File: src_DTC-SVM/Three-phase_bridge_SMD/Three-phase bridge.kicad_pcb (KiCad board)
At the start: 2 copper layers, 419.1 x 318 mm, 92 parts, among them M1 MCP6022-I/P, M2 MCP6022-I/P, P1 CONN_1, P2 POWER_FUSE, P3 CONN_2, P4 CONN_1, P5 CONN_1, P6 POWER_FUSE

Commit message: Commiting...
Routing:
- net +48V: track 185.1 -> 276.9 mm
- net N-0000026: track 18.3 -> 63.0 mm, vias 0 -> 1
- net GND: track 489.9 -> 506.0 mm
- net VCC: track 140.0 -> 146.8 mm
- net N-0000046: track 0.00 -> 2.17 mm
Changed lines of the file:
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@@
   (general
     (links 262)
-    (no_connects 55)
+    (no_connects 50)
     (area -125.780001 -108.254001 293.420001 219.695888)
     (thickness 1.6)
     (drawings 8)
-    (tracks 821)
+    (tracks 855)
     (zones 0)
     (modules 92)
@@
   (segment (start 179.197 116.713) (end 179.197 127.381) (width 1.905) (layer B.Cu) (net 1))
   (segment (start 178.181 115.697) (end 179.197 116.713) (width 1.905) (layer B.Cu) (net 1))
+  (segment (start 217.297 94.869) (end 218.059 94.869) (width 1.905) (layer F.Cu) (net 2))
+  (segment (start 216.154 93.726) (end 217.297 94.869) (width 1.905) (layer F.Cu) (net 2) (status 400000))
+  (segment (start 215.265 93.726) (end 216.154 93.726) (width 1.905) (layer F.Cu) (net 2) (status C00000))
+  (segment (start 218.059 94.869) (end 221.7674 91.1606) (width 1.905) (layer F.Cu) (net 2))
+  (segment (start 215.265 93.726) (end 216.789 93.726) (width 1.905) (layer F.Cu) (net 2) (status 400000))
+  (segment (start 221.7674 92.837) (end 221.7674 93.7006) (width 1.905) (layer F.Cu) (net 2))
+  (segment (start 217.678 92.837) (end 221.7674 92.837) (width 1.905) (layer F.Cu) (net 2))
+  (segment (start 216.789 93.726) (end 217.678 92.837) (width 1.905) (layer F.Cu) (net 2))
+  (segment (start 221.7674 93.7006) (end 221.7674 93.7006) (width 1.905) (layer F.Cu) (net 2))
+  (segment (start 220.218 86.741) (end 220.853 86.741) (width 7.62) (layer F.Cu) (net 2))
+  (segment (start 220.853 86.741) (end 221.7674 87.6554) (width 7.62) (layer F.Cu) (net 2))
+  (segment (start 221.7674 87.6554) (end 221.7674 91.1606) (width 7.62) (layer F.Cu) (net 2))
+  (segment (start 182.8546 71.7296) (end 152.4762 71.7296) (width 7.62) (layer F.Cu) (net 2) (status 800000))
+  (segment (start 220.218 86.487) (end 220.218 86.741) (width 7.62) (layer F.Cu) (net 2))
+  (segment (start 217.932 84.201) (end 220.218 86.487) (width 7.62) (layer F.Cu) (net 2))
+  (segment (start 195.326 84.201) (end 217.932 84.201) (width 7.62) (layer F.Cu) (net 2))
+  (segment (start 182.8546 71.7296) (end 195.326 84.201) (width 7.62) (layer F.Cu) (net 2))
+  (segment (start 221.7674 91.1606) (end 221.7674 93.7006) (width 7.62) (layer F.Cu) (net 2))
   (segment (start 133.3754 80.0862) (end 134.4676 80.0862) (width 1.016) (layer F.Cu) (net 2))
   (segment (start 134.9248 79.629) (end 134.9248 74.0156) (width 1.016) (layer F.Cu) (net 2))
@@
   (segment (start 134.9248 74.0156) (end 134.9248 75.2348) (width 1.016) (layer F.Cu) (net 2))
   (segment (start 134.747 70.739) (end 134.9248 70.9168) (width 1.016) (layer F.Cu) (net 2))
-  (segment (start 221.742 93.6752) (end 215.3158 93.6752) (width 1.905) (layer F.Cu) (net 2))
-  (segment (start 215.3158 93.6752) (end 215.265 93.726) (width 1.905) (layer F.Cu) (net 2))
-  (segment (start 221.742 93.6752) (end 221.7674 93.7006) (width 7.62) (layer F.Cu) (net 2))
   (segment (start 234.696 205.867) (end 234.696 204.216) (width 1.905) (layer F.Cu) (net 2))
   (segment (start 233.045 202.565) (end 226.949 202.565) (width 1.905) (layer F.Cu) (net 2))
@@
   (segment (start 191.3763 199.0217) (end 191.3763 202.4253) (width 1.905) (layer F.Cu) (net 3))
   (segment (start 191.3763 202.4253) (end 191.4525 202.5015) (width 1.905) (layer F.Cu) (net 3))
+  (segment (start 194.818 113.5126) (end 194.818 112.903) (width 1.016) (layer F.Cu) (net 4) (status 400000))
+  (segment (start 186.2582 106.6038) (end 186.2582 108.0516) (width 1.016) (layer F.Cu) (net 4) (status 800000))
+  (segment (start 186.563 106.299) (end 186.2582 106.6038) (width 1.016) (layer F.Cu) (net 4))
+  (segment (start 192.659 106.299) (end 186.563 106.299) (width 1.016) (layer F.Cu) (net 4))
+  (segment (start 193.294 106.934) (end 192.659 106.299) (width 1.016) (layer F.Cu) (net 4))
+  (segment (start 193.294 111.379) (end 193.294 106.934) (width 1.016) (layer F.Cu) (net 4))
+  (segment (start 194.818 112.903) (end 193.294 111.379) (width 1.016) (layer F.Cu) (net 4))
   (segment (start 183.388 101.727) (end 183.388 107.315) (width 1.016) (layer B.Cu) (net 4) (status 400000))
   (segment (start 183.388 107.315) (end 184.15 108.077) (width 1.016) (layer B.Cu) (net 4) (status 800000))
@@
   (segment (start 174.9171 205.3209) (end 177.43424 205.3209) (width 1.905) (layer F.Cu) (net 11))
   (segment (start 177.43424 205.3209) (end 177.4571 205.34376) (width 1.905) (layer F.Cu) (net 11))
-  (segment (start 150.8252 123.8504) (end 150.8252 120.3198) (width 1.905) (layer F.Cu) (net 12))
-  (segment (start 150.8252 120.3198) (end 152.146 118.999) (width 1.905) (layer F.Cu) (net 12))
+  (segment (start 150.8252 123.8504) (end 150.8252 120.3198) (width 1.905) (layer F.Cu) (net 12) (status C00000))
+  (segment (start 150.8252 120.3198) (end 152.146 118.999) (width 1.905) (layer F.Cu) (net 12) (status C00000))
   (segment (start 166.6367 205.34376) (end 163.99256 205.34376) (width 1.905) (layer F.Cu) (net 13))
   (segment (start 163.99256 205.34376) (end 163.9697 205.3209) (width 1.905) (layer F.Cu) (net 13))
@@
   (segment (start 186.4106 125.73) (end 186.6138 125.9332) (width 1.905) (layer F.Cu) (net 26))
   (segment (start 186.6138 125.9332) (end 188.5696 125.9332) (width 1.905) (layer F.Cu) (net 26))
+  (via (at 197.739 128.016) (size 0.254) (layers F.Cu B.Cu) (net 27))
+  (segment (start 194.818 121.8946) (end 196.1896 121.8946) (width 1.016) (layer F.Cu) (net 27) (status 400000))
+  (segment (start 196.1896 121.8946) (end 197.739 123.444) (width 1.016) (layer F.Cu) (net 27))
+  (segment (start 197.739 128.016) (end 197.739 123.444) (width 1.905) (layer F.Cu) (net 27))
+  (segment (start 206.756 151.257) (end 206.756 160.909) (width 1.905) (layer B.Cu) (net 27) (status 800000))
+  (segment (start 200.152 144.653) (end 206.756 151.257) (width 1.905) (layer B.Cu) (net 27))
+  (segment (start 200.152 130.429) (end 200.152 144.653) (width 1.905) (layer B.Cu) (net 27))
+  (segment (start 197.739 128.016) (end 200.152 130.429) (width 1.905) (layer B.Cu) (net 27))
   (segment (start 199.644 163.449) (end 204.216 163.449) (width 1.016) (layer B.Cu) (net 27))
   (segment (start 204.216 163.449) (end 206.756 160.909) (width 1.016) (layer B.Cu) (net 27))
@@
   (segment (start 154.432 186.563) (end 165.8576 186.563) (width 0.889) (layer B.Cu) (net 48))
   (segment (start 153.1355 185.2665) (end 154.432 186.563) (width 0.889) (layer B.Cu) (net 48))
+  (segment (start 158.877 104.54386) (end 161.01314 104.54386) (width 1.905) (layer F.Cu) (net 49) (status C00000))
+  (segment (start 161.01314 104.54386) (end 161.036 104.521) (width 1.905) (layer F.Cu) (net 49) (status C00000))
   (segment (start 194.691 104.267) (end 196.215 104.267) (width 1.016) (layer B.Cu) (net 50))
   (segment (start 196.215 104.267) (end 200.533 108.585) (width 1.016) (layer B.Cu) (net 50))
@@
   (segment (start 207.6196 148.3614) (end 208.534 147.447) (width 1.905) (layer F.Cu) (net 91))
   (segment (start 188.9506 138.2522) (end 184.3786 138.2522) (width 1.905) (layer F.Cu) (net 92))
+  (segment (start 158.877 101.70414) (end 152.16886 101.70414) (width 1.905) (layer F.Cu) (net 93) (status C00000))
+  (segment (start 152.16886 101.70414) (end 152.146 101.727) (width 1.905) (layer F.Cu) (net 93) (status C00000))
   (segment (start 168.1988 120.4214) (end 168.783 120.4214) (width 1.905) (layer F.Cu) (net 93))
   (segment (start 181.9402 141.5796) (end 183.6928 143.3322) (width 1.905) (layer F.Cu) (net 93))

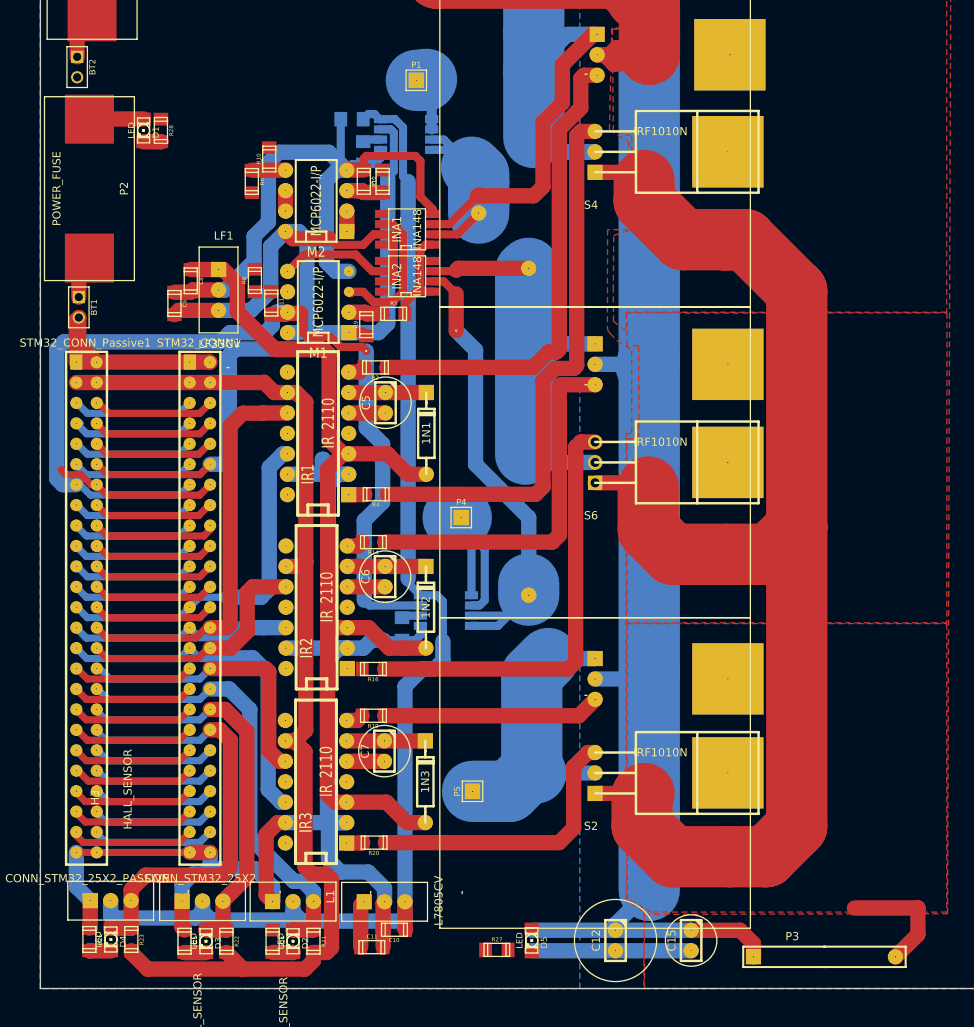
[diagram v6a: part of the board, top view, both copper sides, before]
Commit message: New ADC ports for the hall current sensors have been added to the PCB. Rewiring of surrounding connections is being carried out.
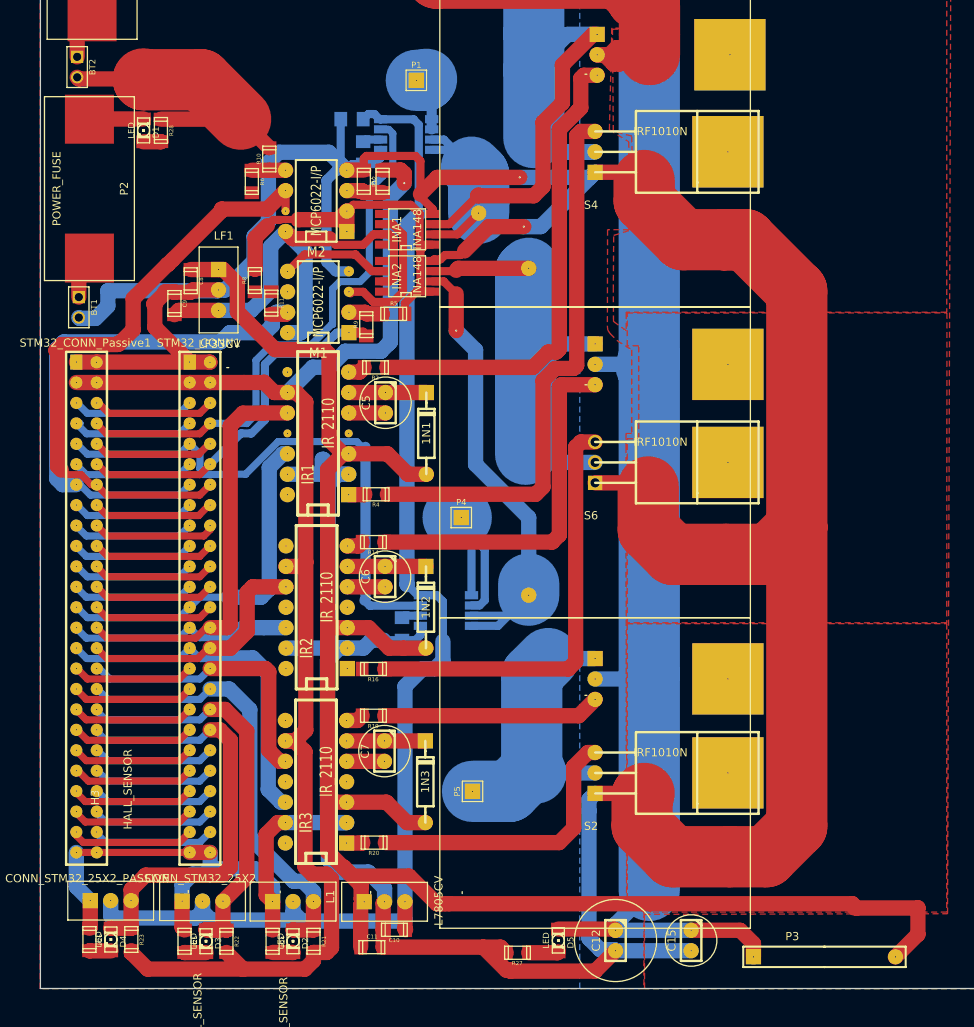
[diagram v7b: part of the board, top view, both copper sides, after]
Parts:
- moved D5 3.30 mm to (210.4, 203.8)
- moved R27 2.59 mm to (205.4, 205.4), turned to 180 degrees
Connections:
- ACS1 pad 7: N-0000065 (its old number) -> N-0000066
- ACS2 pad 7: N-0000034 (its old number) -> N-0000048
- M1 pad 1: N-0000065 (its old number) -> N-0000067
- M1 pad 7: N-0000034 (its old number) -> N-0000037
- R11 pad 1: N-0000034 (its old number) -> N-0000037
- R9 pad 2: N-0000065 (its old number) -> N-0000067
- STM32_CONN1 pad 12: N-0000065 (its old number) -> N-0000067
- STM32_CONN1 pad 13: N-0000034 (its old number) -> N-0000037
- STM32_CONN1 pad 8: N-0000064 (its old number) -> N-0000066
- STM32_CONN1 pad 9: N-0000037 -> N-0000048
- STM32_CONN_Passive1 pad 12: N-0000065 (its old number) -> N-0000067
- STM32_CONN_Passive1 pad 13: N-0000034 (its old number) -> N-0000037
- STM32_CONN_Passive1 pad 8: N-0000064 (its old number) -> N-0000066
- STM32_CONN_Passive1 pad 9: N-0000037 -> N-0000048
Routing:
- net GND: track 506.0 -> 661.5 mm, vias 0 -> 2
- net N-0000034 (its old number): track 120.5 -> 0.00 mm, vias 1 -> 0
- net VCC: track 146.8 -> 228.0 mm
- net N-0000065 (its old number): track 80.3 -> 0.00 mm
- net N-0000066: track 0.00 -> 69.5 mm
- net N-0000048: track 0.00 -> 68.7 mm
- net N-0000039: track 23.0 -> 77.4 mm
- net N-0000037: track 15.2 -> 67.4 mm
- net N-0000067: track 0.00 -> 45.6 mm
- net VDD: track 168.1 -> 208.2 mm, vias 0 -> 1
- net N-0000087: track 15.1 -> 46.2 mm
- net N-0000064 (its old number): track 15.2 -> 0.00 mm
- net N-0000058: track 0.00 -> 3.73 mm
- net +48V: track 276.9 -> 273.7 mm
- net +5V: track 158.5 -> 161.3 mm
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- added copper zone on F.Cu, net N-000006
- added copper zone on F.Cu, net N-0000061
- added copper zone on F.Cu, net N-0000062
- removed copper zone on F.Cu, net N-000002
- removed copper zone on F.Cu, net N-0000063
- removed copper zone on F.Cu, net N-0000064

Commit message: Adding fillzones to the PCB.
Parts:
- C20: moved to B.Cu
- moved C16 192.2 mm to (194.3, 206.6), turned to 90 degrees
- moved C17 191.9 mm to (187.3, 206.6), turned to 90 degrees
- moved C1 167.9 mm to (245.9, 204.6)
- moved C4 151.8 mm to (200.1, 178.8), turned to 0 degrees
- moved C2 151.5 mm to (201.1, 167.2), turned to 0 degrees
- moved P3 139.3 mm to (165.1, 91.2), turned to 270 degrees
- moved C3 132.7 mm to (237.2, 204.6)
- moved C13 82.6 mm to (245.6, 125.5), turned to 270 degrees
- moved C14 81.7 mm to (245.6, 116.6)
- moved R13 54.7 mm to (184.6, 90.7)
- moved R18 54.7 mm to (184.5, 97.5)
- moved R15 54.7 mm to (184.6, 92.8)
- moved R17 54.7 mm to (184.5, 95.2)
- moved RGL2 54.7 mm to (179.5, 91.7)
- moved RGL3 54.7 mm to (179.4, 96.4)
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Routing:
- net GND: track 661.5 -> 912.8 mm, vias 2 -> 6
- net N-000004: track 41.4 -> 246.8 mm, vias 0 -> 2
- net +48V: track 273.7 -> 385.8 mm
- net N-0000029: track 64.7 -> 119.3 mm, vias 0 -> 1
- net N-0000012: track 103.8 -> 146.1 mm
- net VCC: track 228.0 -> 254.2 mm, vias 1 -> 2
- net (no net): track 23.4 -> 0.00 mm, vias 1 -> 0
- net VDD: track 208.2 -> 199.8 mm
- net N-000001: track 44.1 -> 41.1 mm
- net N-0000048: track 68.7 -> 71.4 mm
- net +5V: track 161.3 -> 163.2 mm
- added copper zone on B.Cu, net GND
- removed copper zone on F.Cu, net +48V
- removed copper zone on F.Cu, net GND
- removed copper zone on F.Cu, net N-000006
- removed copper zone on F.Cu, net N-0000061
- removed copper zone on F.Cu, net N-0000062
